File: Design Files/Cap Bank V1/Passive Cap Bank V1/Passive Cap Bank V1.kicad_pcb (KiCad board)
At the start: 2 copper layers, 66.4 x 115.9 mm, 38 parts, among them J1 XT30-Male, Q1 BC817-40, Q2 BC817-40, Q3 BC817-40, Q4 BC817-40, Q5 BC817-40, Q6 BC817-40, SW1 SW_Push_Open

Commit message: mech finalized
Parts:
- moved REF** 0.65 mm to (130.6, 32.2)
- moved REF** 0.62 mm to (189.8, 32.2)
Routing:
- net (no net): vias 2 -> 0
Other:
- outline, holes or cut-outs redrawn

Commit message: final
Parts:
- moved C4 15.3 mm to (147.5, 141.6)
- moved Q4 15.3 mm to (143.6, 141.6)
- moved REF** 15.3 mm to (178.9, 150.9)
- moved C5 15.3 mm to (147.4, 121.7)
- moved C6 15.3 mm to (147.5, 101.9)
- moved D1 15.3 mm to (154.7, 84.9)
- moved J1 15.3 mm to (178.1, 82.7)
- moved Q5 15.3 mm to (143.5, 121.7)
- moved Q6 15.3 mm to (143.4, 101.7)
- moved R1 15.3 mm to (173.7, 98.1)
- moved R10 15.3 mm to (141.3, 117.6)
- moved R11 15.3 mm to (141.3, 106.5)
- moved R12 15.3 mm to (141.3, 97.5)
- moved R13 15.3 mm to (143.1, 83.3)
- moved R3 15.3 mm to (173.8, 117.7)
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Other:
- outline, holes or cut-outs redrawn
- board text added: "Caution! Device hot while discharging!"
- board text added: "Lick here"

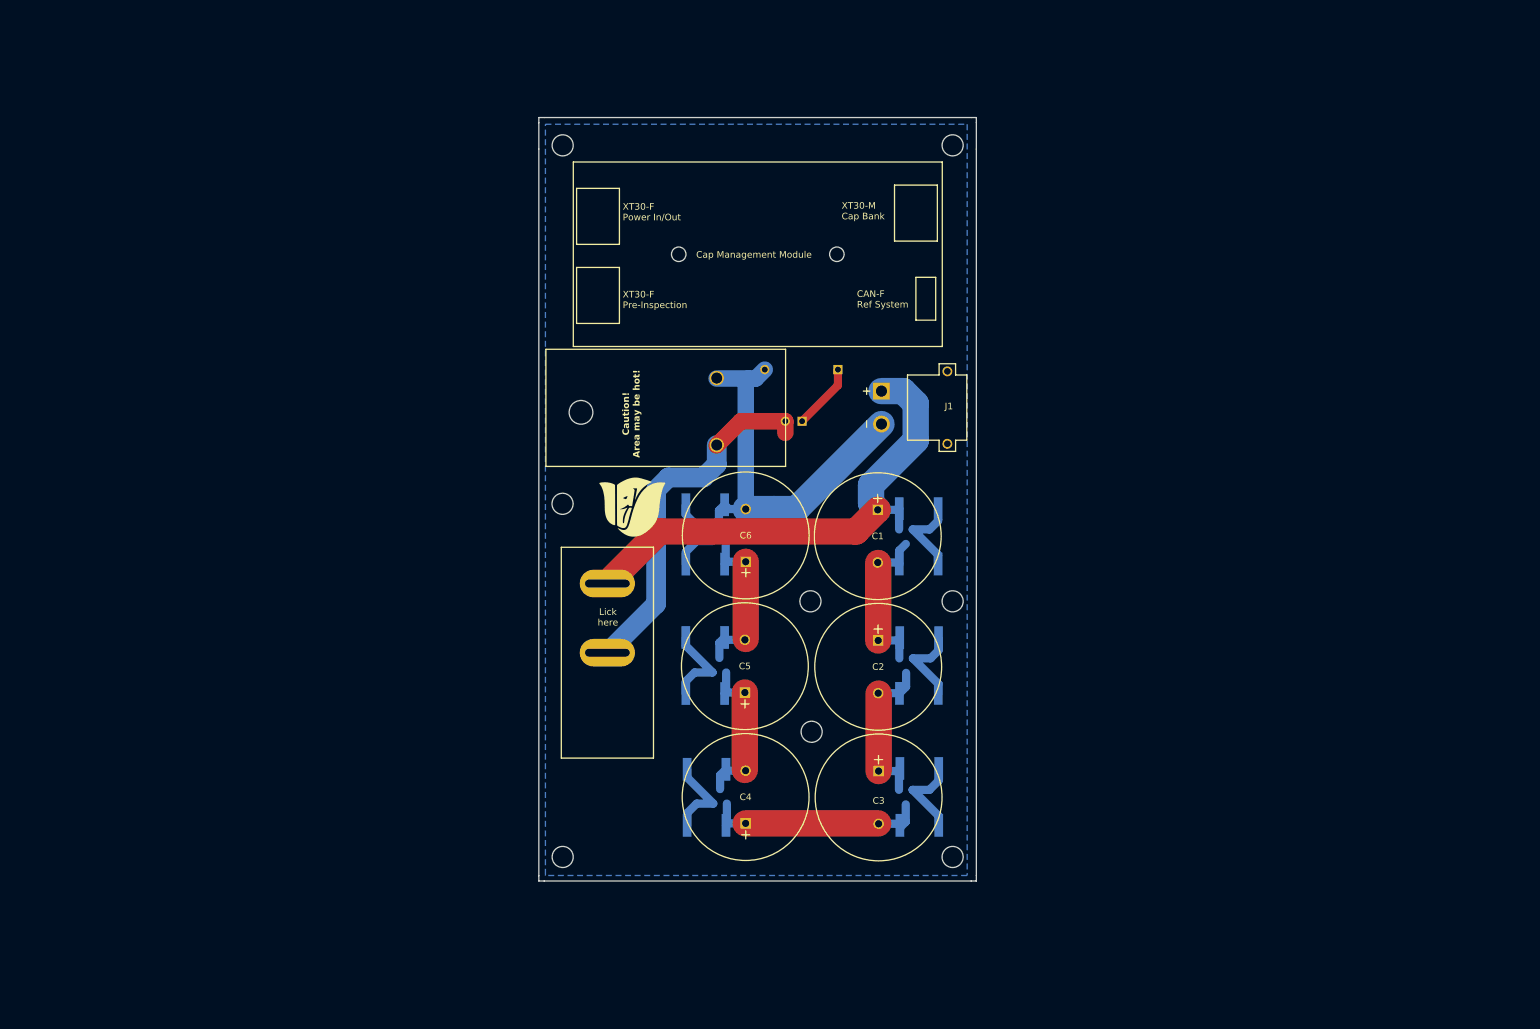
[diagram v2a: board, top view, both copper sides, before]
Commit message: Changing to the new capacitor footprints. Redoing layout.
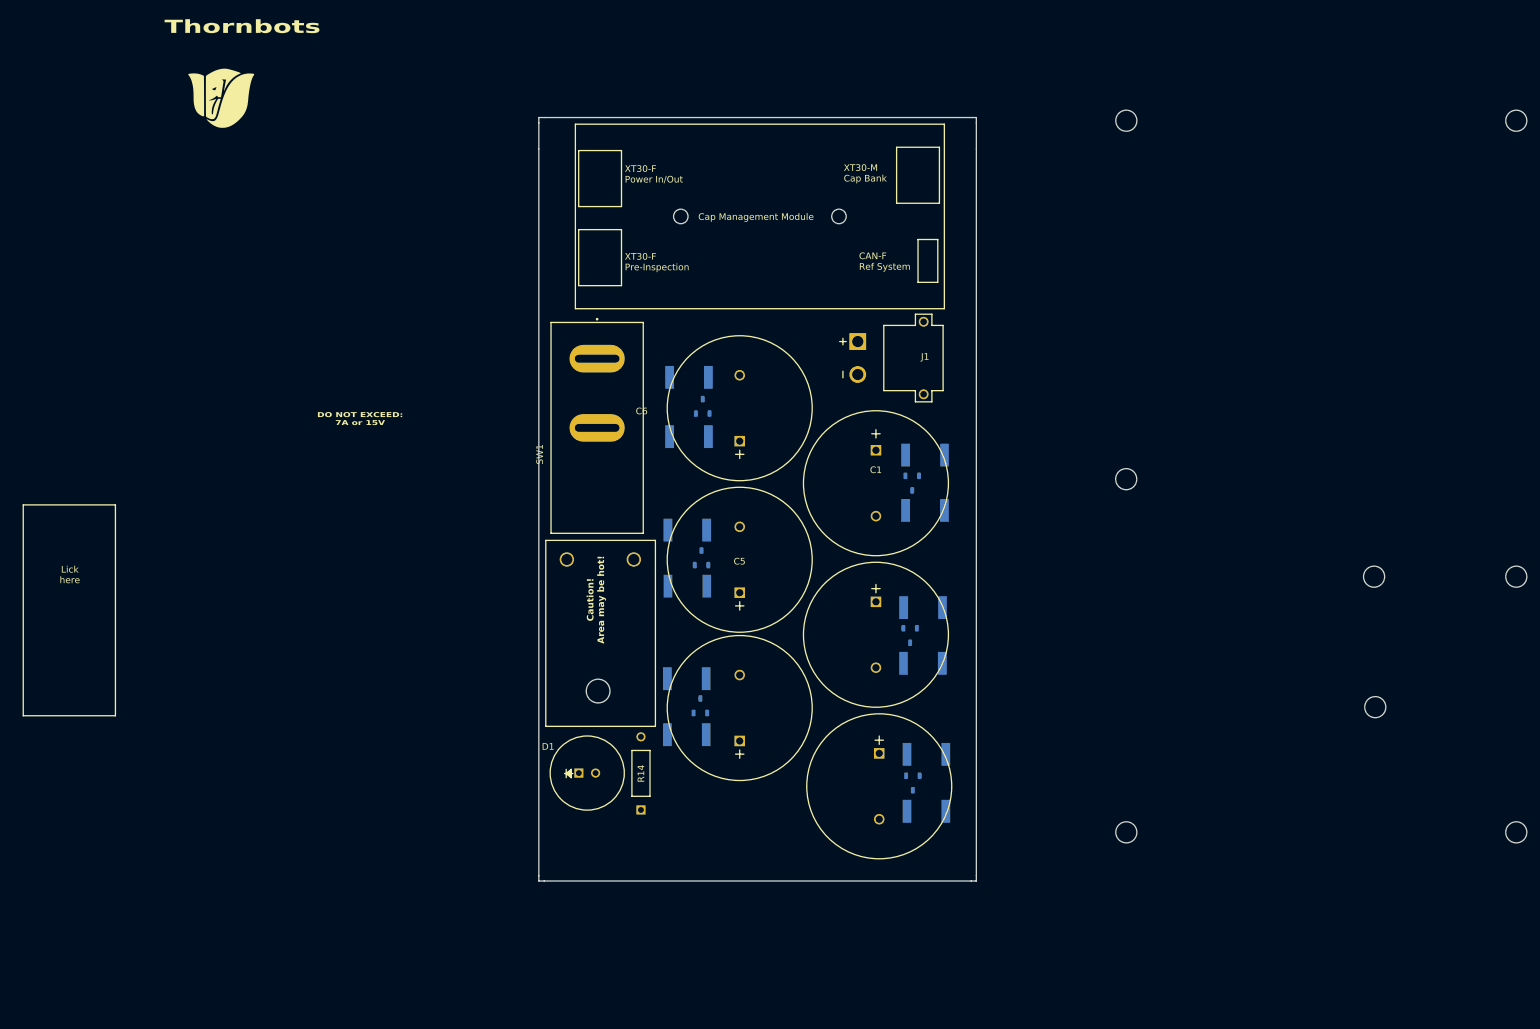
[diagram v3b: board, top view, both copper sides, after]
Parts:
- added G***: LOGO, PassiveBankV1:10mm RM Logo, B.Cu at (86.2, 36.0)
- D1, R14, SW1: moved to F.Cu
- moved G*** 88.0 mm to (67.9, 35.8)
- moved REF** 85.6 mm to (243.0, 128.2)
- moved REF** 85.6 mm to (205.2, 39.2)
- moved REF** 85.6 mm to (205.2, 93.6)
- moved REF** 85.6 mm to (205.2, 147.2)
- moved REF** 85.6 mm to (264.4, 39.2)
- moved REF** 85.6 mm to (264.4, 147.2)
- moved REF** 85.6 mm to (242.8, 108.4)
- moved REF** 85.6 mm to (264.4, 108.4)
- moved R14 66.1 mm to (131.5, 138.4), turned to 90 degrees
- moved D1 61.8 mm to (123.5, 138.3), turned to 0 degrees
- moved SW1 34.2 mm to (124.9, 85.8)
- moved R13 28.6 mm to (125.4, 105.8), turned to 0 degrees
- moved Q6 19.5 mm to (140.9, 82.4)
- moved R11 19.5 mm to (138.9, 87.1)
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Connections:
- C2 pad 1: Net-(C1--) -> (no net)
- C2 pad 2: Net-(C2--) -> (no net)
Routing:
- net V_15: track 77.5 -> 0.00 mm
- net GND: track 60.9 -> 0.00 mm
- net Net-(D1-A): track 55.2 -> 0.00 mm
- net Net-(C3--): track 33.9 -> 0.00 mm
- net Net-(C5--): track 25.7 -> 0.00 mm
- net Net-(C2--): track 25.3 -> 0.00 mm
- net Net-(C1--): track 25.1 -> 0.00 mm
- net Net-(C4--): track 24.8 -> 0.00 mm
- net Net-(Q3-B): track 13.8 -> 0.00 mm
- net Net-(Q6-B): track 13.7 -> 0.00 mm
- net Net-(Q5-B): track 13.5 -> 0.00 mm
- net Net-(Q4-B): track 13.3 -> 0.00 mm
- net Net-(Q2-B): track 13.2 -> 0.00 mm
- net Net-(Q1-B): track 13.1 -> 0.00 mm
- net Net-(D1-K): track 10.1 -> 0.00 mm
- removed copper zone on B.Cu, net (none)
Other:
- outline, holes or cut-outs redrawn
- board text added: "DO NOT EXCEED: 7A or 15V"
- board text added: "Designed by Rose-Hulman Thornbots, 2024-2025 https://github.com/Thornbots/Supa-Cap Passive Cap Bank V1"
- board text added: "Thornbots"
- board text removed: "Caution! Device hot while discharging!"
- board text removed: "DO NOT EXCEED: 7A or 15V YOU WILL BLOW UP A TRACE OR A CAPACITOR Use at your own risk"
- board text removed: "Designed by Rose-Hulman Thornbots, October 2024 https://github.com/Thornbots/Supa-Cap Passive Cap Bank V1"

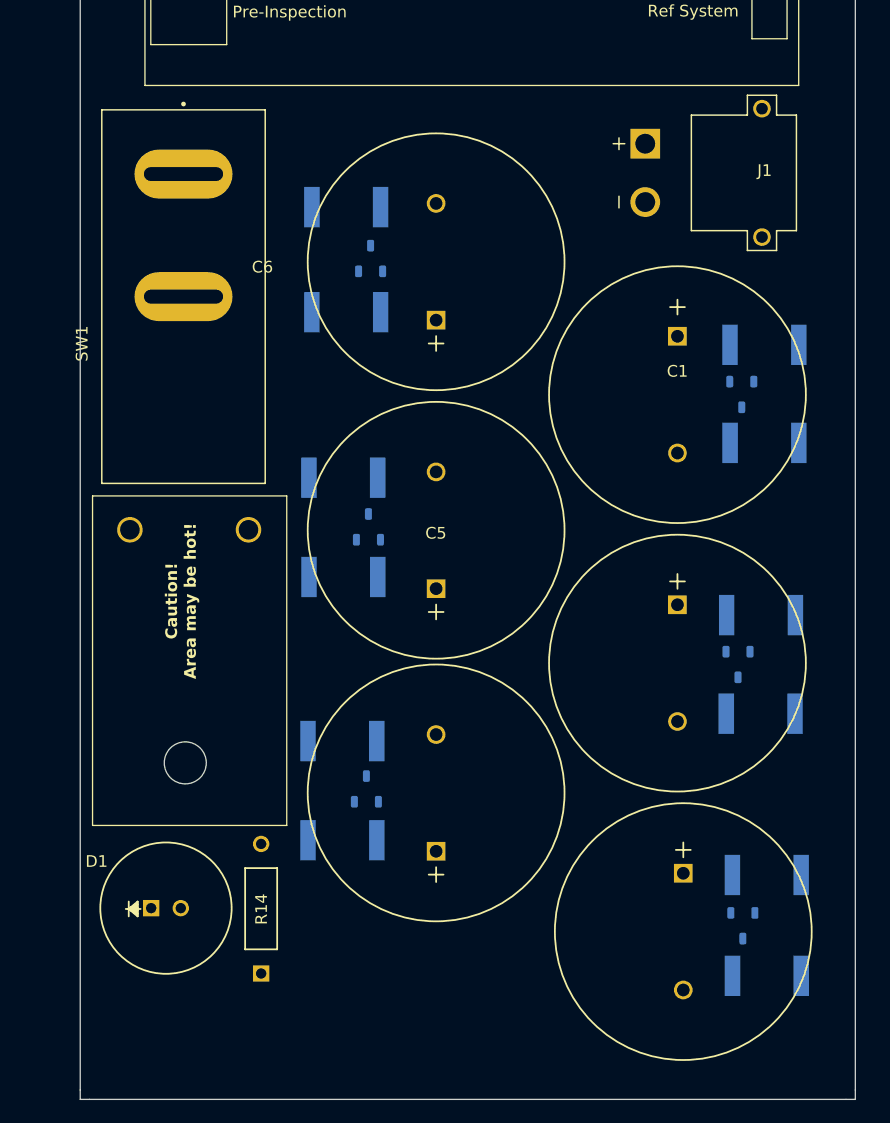
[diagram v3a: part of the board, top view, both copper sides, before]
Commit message: Improved Layout and started routing
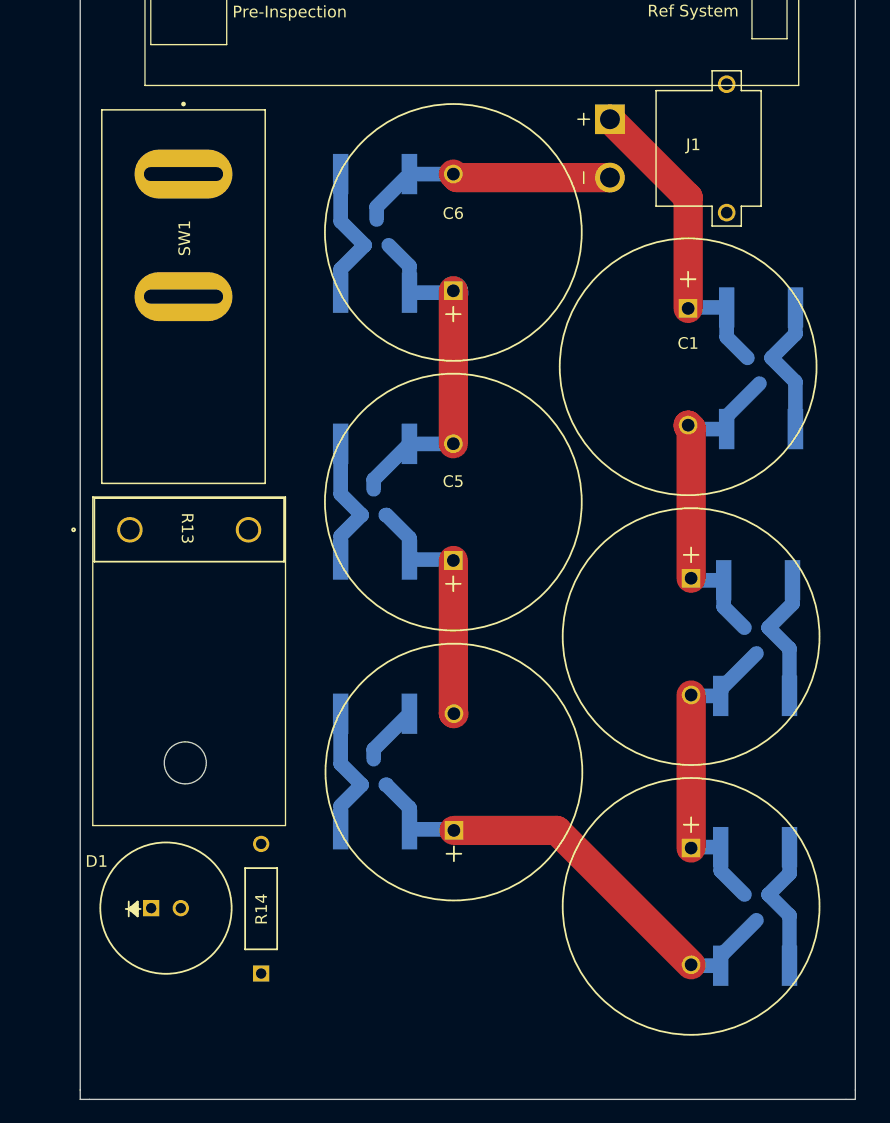
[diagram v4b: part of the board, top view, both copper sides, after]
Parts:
- R13: moved to F.Cu
- moved R10 3.98 mm to (141.3, 98.4)
- moved R12 3.76 mm to (141.3, 75.3)
- moved J1 3.68 mm to (171.4, 73.1)
- moved R8 3.65 mm to (141.3, 121.5)
- moved R1 3.21 mm to (174.4, 86.7)
- moved R9 3.10 mm to (141.3, 108.3)
- moved R3 2.99 mm to (174.1, 110.1)
- moved R11 2.98 mm to (141.3, 85.5)
- moved R7 2.95 mm to (141.3, 131.4)
- moved C6 2.92 mm to (148.0, 80.3)
- moved C5 2.83 mm to (148.0, 103.4)
- moved Q2 2.59 mm to (174.0, 115.4)
- moved R5 2.59 mm to (173.9, 133.0)
- moved C1 2.56 mm to (168.1, 91.8)
- moved C2 2.56 mm to (168.4, 114.9)
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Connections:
- C2 pad 1: (no net) -> Net-(C1--)
- C2 pad 2: (no net) -> Net-(C2--)
- R13 pad 3: GND -> (no net)
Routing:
- net Net-(C3--): track 0.00 -> 41.4 mm
- net Net-(C5--): track 0.00 -> 30.8 mm
- net Net-(C1--): track 0.00 -> 29.5 mm
- net Net-(C2--): track 0.00 -> 28.1 mm
- net V_15: track 0.00 -> 27.4 mm
- net Net-(C4--): track 0.00 -> 26.8 mm
- net GND: track 0.00 -> 22.4 mm
- net Net-(Q1-B): track 0.00 -> 12.1 mm
- net Net-(Q6-B): track 0.00 -> 11.9 mm
- net Net-(Q3-B): track 0.00 -> 11.6 mm
- net Net-(Q2-B): track 0.00 -> 11.5 mm
- net Net-(Q5-B): track 0.00 -> 11.4 mm
- net Net-(Q4-B): track 0.00 -> 11.4 mm
